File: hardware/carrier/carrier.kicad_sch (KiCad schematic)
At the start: 8 parts

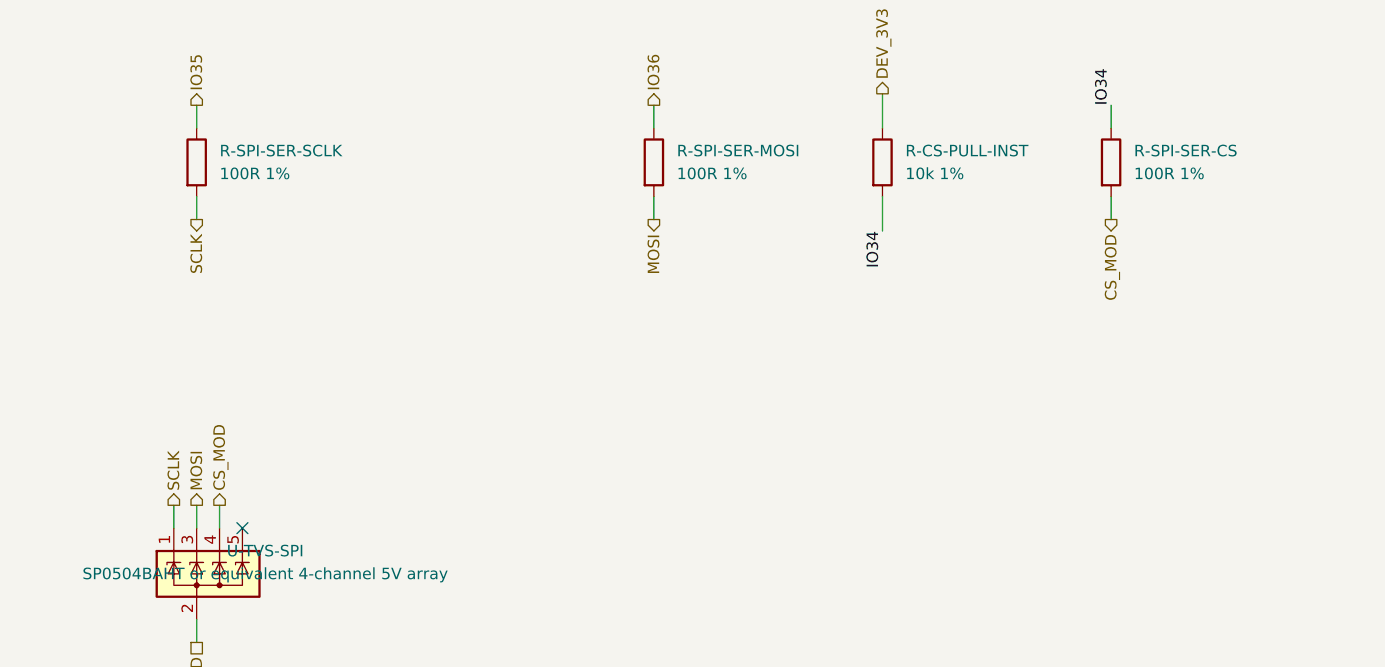
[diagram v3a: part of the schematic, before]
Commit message: WIP SPI link: U-TVS-SPI to the pad side, R-SPI-SER 82R; module receiver U-RX-MOD (74AHCT14) behind R-RX-MOD/C-RX-MOD
Co-Authored-By: Claude Opus 5.5 <noreply@anthropic.com>
Claude-Session: https://claude.ai/code/session_01LmB4muFXnoLprWX4JzuJ5A
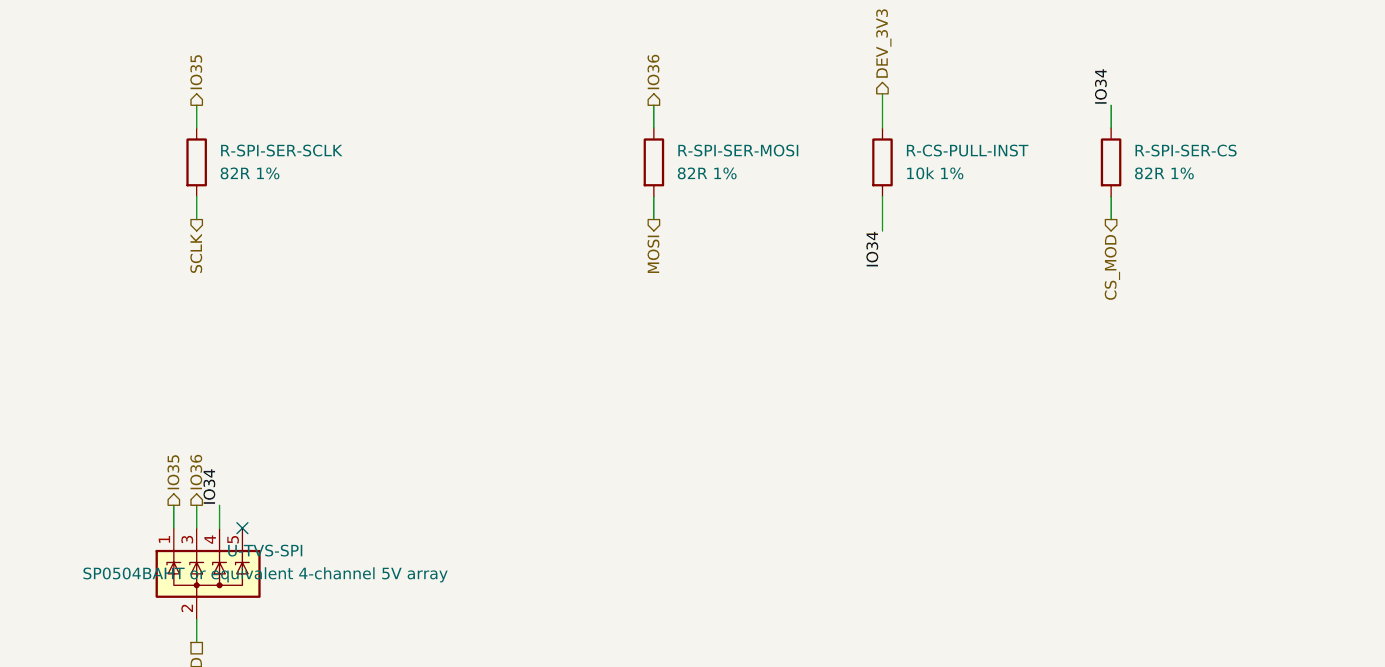
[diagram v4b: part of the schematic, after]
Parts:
- R-SPI-SER-CS, R-SPI-SER-MOSI: value 100R 1% -> 82R 1%; LCSC C17901 -> C17980; MPN 1206W4F1000T5E -> 1206W4F820JT5E
- R-SPI-SER-SCLK: value 100R 1% -> 82R 1%; LCSC C17901 -> C17980; MPN 1206W4F1000T5E -> 1206W4F820JT5E; Note At the DRIVING end, which is this board. The far end's thre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 -> At the DRIVING end, which is this board, with U-TVS-SPI on 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
- U-TVS-SPI: Note On the umbilical side of the series resistors, where the ca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 -> On the MCU side of R-SPI-SER, at the pads (owner, 2026-09-3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
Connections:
- net CS_MOD: no longer U-TVS-SPI.4 (K)
- net IO34: now also U-TVS-SPI.4 (K)
- net IO35: now also U-TVS-SPI.1 (K)
- net IO36: now also U-TVS-SPI.3 (K)
- net MOSI: no longer U-TVS-SPI.3 (K)
- net SCLK: no longer U-TVS-SPI.1 (K)
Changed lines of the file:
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@@
     (in_bom yes) (on_board yes) (dnp no)
     (property "Reference" "R-SPI-SER-SCLK" (at 43.18 232.41 0) (effects (font (size 1.27 1.27)) (justify left)))
-    (property "Value" "100R 1%" (at 43.18 234.95 0) (effects (font (size 1.27 1.27)) (justify left)))
+    (property "Value" "82R 1%" (at 43.18 234.95 0) (effects (font (size 1.27 1.27)) (justify left)))
     (property "Footprint" "Resistor_SMD:R_1206_3216Metric" (at 39.37 233.68 0) (effects (font (size 1.27 1.27)) hide))
     (property "Datasheet" "" (at 40.64 233.68 0) (effects (font (size 1.27 1.27)) hide))
@@
     (property "Pins" "1=1 2=2" (at 40.64 233.68 0) (effects (font (size 1.27 1.27)) hide))
     (property "Drawn_as" "R-SPI-SER" (at 40.64 233.68 0) (effects (font (size 1.27 1.27)) hide))
-    (property "Note" "At the DRIVING end, which is this board. The far end's threshold is the 74AHCT125's TTL V_IH, not a ratio of its rail" (at 40.64 233.68 0) (effects (font (size 1.27 1.27)) hide))
+    (property "Note" "At the DRIVING end, which is this board, with U-TVS-SPI on its pad side. The far end's receiver is the module's Schmitt stage, U-RX-MOD (74AHCT14): TTL thresholds, not a ratio of its rail" (at 40.64 233.68 0) (effects (font (size 1.27 1.27)) hide))
     (property "Manufacturer" "UNI-ROYAL" (at 40.64 233.68 0) (effects (font (size 1.27 1.27)) hide))
-    (property "MPN" "1206W4F1000T5E" (at 40.64 233.68 0) (effects (font (size 1.27 1.27)) hide))
-    (property "LCSC" "C17901" (at 40.64 233.68 0) (effects (font (size 1.27 1.27)) hide))
+    (property "MPN" "1206W4F820JT5E" (at 40.64 233.68 0) (effects (font (size 1.27 1.27)) hide))
+    (property "LCSC" "C17980" (at 40.64 233.68 0) (effects (font (size 1.27 1.27)) hide))
     (property "Assembly" "machine" (at 40.64 233.68 0) (effects (font (size 1.27 1.27)) hide))
     (pin "1")
@@
     (in_bom yes) (on_board yes) (dnp no)
     (property "Reference" "R-SPI-SER-MOSI" (at 93.98 232.41 0) (effects (font (size 1.27 1.27)) (justify left)))
-    (property "Value" "100R 1%" (at 93.98 234.95 0) (effects (font (size 1.27 1.27)) (justify left)))
+    (property "Value" "82R 1%" (at 93.98 234.95 0) (effects (font (size 1.27 1.27)) (justify left)))
     (property "Footprint" "Resistor_SMD:R_1206_3216Metric" (at 90.17 233.68 0) (effects (font (size 1.27 1.27)) hide))
     (property "Datasheet" "" (at 91.44 233.68 0) (effects (font (size 1.27 1.27)) hide))
@@
     (property "Pins" "1=1 2=2" (at 91.44 233.68 0) (effects (font (size 1.27 1.27)) hide))
     (property "Manufacturer" "UNI-ROYAL" (at 91.44 233.68 0) (effects (font (size 1.27 1.27)) hide))
-    (property "MPN" "1206W4F1000T5E" (at 91.44 233.68 0) (effects (font (size 1.27 1.27)) hide))
-    (property "LCSC" "C17901" (at 91.44 233.68 0) (effects (font (size 1.27 1.27)) hide))
+    (property "MPN" "1206W4F820JT5E" (at 91.44 233.68 0) (effects (font (size 1.27 1.27)) hide))
+    (property "LCSC" "C17980" (at 91.44 233.68 0) (effects (font (size 1.27 1.27)) hide))
     (property "Assembly" "machine" (at 91.44 233.68 0) (effects (font (size 1.27 1.27)) hide))
     (pin "1")
@@
     (in_bom yes) (on_board yes) (dnp no)
     (property "Reference" "R-SPI-SER-CS" (at 144.78 232.41 0) (effects (font (size 1.27 1.27)) (justify left)))
-    (property "Value" "100R 1%" (at 144.78 234.95 0) (effects (font (size 1.27 1.27)) (justify left)))
+    (property "Value" "82R 1%" (at 144.78 234.95 0) (effects (font (size 1.27 1.27)) (justify left)))
     (property "Footprint" "Resistor_SMD:R_1206_3216Metric" (at 140.97 233.68 0) (effects (font (size 1.27 1.27)) hide))
     (property "Datasheet" "" (at 142.24 233.68 0) (effects (font (size 1.27 1.27)) hide))
@@
     (property "Pins" "1=1 2=2" (at 142.24 233.68 0) (effects (font (size 1.27 1.27)) hide))
     (property "Manufacturer" "UNI-ROYAL" (at 142.24 233.68 0) (effects (font (size 1.27 1.27)) hide))
-    (property "MPN" "1206W4F1000T5E" (at 142.24 233.68 0) (effects (font (size 1.27 1.27)) hide))
-    (property "LCSC" "C17901" (at 142.24 233.68 0) (effects (font (size 1.27 1.27)) hide))
+    (property "MPN" "1206W4F820JT5E" (at 142.24 233.68 0) (effects (font (size 1.27 1.27)) hide))
+    (property "LCSC" "C17980" (at 142.24 233.68 0) (effects (font (size 1.27 1.27)) hide))
     (property "Assembly" "machine" (at 142.24 233.68 0) (effects (font (size 1.27 1.27)) hide))
     (pin "1")
@@
     (property "Row" "U-TVS-SPI" (at 40.64 279.4 0) (effects (font (size 1.27 1.27)) hide))
     (property "Pins" "CH1=1(K) CH2=3(K) CH3=4(K) CH4=5(K) GND=2(A)" (at 40.64 279.4 0) (effects (font (size 1.27 1.27)) hide))
-    (property "Note" "On the umbilical side of the series resistors, where the cable's energy arrives" (at 40.64 279.4 0) (effects (font (size 1.27 1.27)) hide))
+    (property "Note" "On the MCU side of R-SPI-SER, at the pads (owner, 2026-09-30): on the line side its capacitance reflected CS_MOD's returning edge back up through the far end's V_IL (cs-fall-reentry, interfaces/spi-link/sim). R-SPI-SER now stands between the cable and the clamp, and limits what a sustained fault on a conductor can push into it" (at 40.64 279.4 0) (effects (font (size 1.27 1.27)) hide))
     (property "Pins_source" "datasheets/discrete-and-power/SP0504BAHT.pdf p.1 pinout (SOT-23-5): I/O on 1, 3, 4, 5, ground on 2" (at 40.64 279.4 0) (effects (font (size 1.27 1.27)) hide))
     (property "Manufacturer" "Littelfuse" (at 40.64 279.4 0) (effects (font (size 1.27 1.27)) hide))
@@
     (property "Figure" "spi-series-r" (at 40.64 240.03 0) (effects (font (size 1.27 1.27)) hide)))
   (wire (pts (xy 38.1 274.32) (xy 38.1 271.78)) (stroke (width 0) (type default)))
-  (hierarchical_label "SCLK" (shape output) (at 38.1 271.78 90) (effects (font (size 1.27 1.27)) (justify left))
+  (hierarchical_label "IO35" (shape output) (at 38.1 271.78 90) (effects (font (size 1.27 1.27)) (justify left))
     (property "Dir" "out" (at 38.1 271.78 0) (effects (font (size 1.27 1.27)) hide))
-    (property "To" "interfaces/spi-link" (at 38.1 271.78 0) (effects (font (size 1.27 1.27)) hide))
-    (property "Figure" "spi-series-r" (at 38.1 271.78 0) (effects (font (size 1.27 1.27)) hide)))
+    (property "To" "carrier/breath-adc" (at 38.1 271.78 0) (effects (font (size 1.27 1.27)) hide)))
   (wire (pts (xy 91.44 237.49) (xy 91.44 240.03)) (stroke (width 0) (type default)))
   (hierarchical_label "MOSI" (shape output) (at 91.44 240.03 270) (effects (font (size 1.27 1.27)) (justify right))
@@
     (property "Figure" "spi-series-r" (at 91.44 240.03 0) (effects (font (size 1.27 1.27)) hide)))
   (wire (pts (xy 40.64 274.32) (xy 40.64 271.78)) (stroke (width 0) (type default)))
-  (hierarchical_label "MOSI" (shape output) (at 40.64 271.78 90) (effects (font (size 1.27 1.27)) (justify left))
+  (hierarchical_label "IO36" (shape output) (at 40.64 271.78 90) (effects (font (size 1.27 1.27)) (justify left))
     (property "Dir" "out" (at 40.64 271.78 0) (effects (font (size 1.27 1.27)) hide))
-    (property "To" "interfaces/spi-link" (at 40.64 271.78 0) (effects (font (size 1.27 1.27)) hide))
-    (property "Figure" "spi-series-r" (at 40.64 271.78 0) (effects (font (size 1.27 1.27)) hide)))
+    (property "To" "carrier/breath-adc" (at 40.64 271.78 0) (effects (font (size 1.27 1.27)) hide)))
   (wire (pts (xy 142.24 237.49) (xy 142.24 240.03)) (stroke (width 0) (type default)))
   (hierarchical_label "CS_MOD" (shape output) (at 142.24 240.03 270) (effects (font (size 1.27 1.27)) (justify right))
@@
     (property "Figure" "spi-series-r" (at 142.24 240.03 0) (effects (font (size 1.27 1.27)) hide)))
   (wire (pts (xy 43.18 274.32) (xy 43.18 271.78)) (stroke (width 0) (type default)))
-  (hierarchical_label "CS_MOD" (shape output) (at 43.18 271.78 90) (effects (font (size 1.27 1.27)) (justify left))
-    (property "Dir" "out" (at 43.18 271.78 0) (effects (font (size 1.27 1.27)) hide))
-    (property "To" "interfaces/spi-link" (at 43.18 271.78 0) (effects (font (size 1.27 1.27)) hide))
-    (property "Figure" "spi-series-r" (at 43.18 271.78 0) (effects (font (size 1.27 1.27)) hide)))
+  (label "IO34" (at 43.18 271.78 90) (fields_autoplaced) (effects (font (size 1.27 1.27)) (justify left bottom)))
   (wire (pts (xy 35.56 55.88) (xy 33.02 55.88)) (stroke (width 0) (type default)))
   (hierarchical_label "IO37" (shape input) (at 33.02 55.88 180) (effects (font (size 1.27 1.27)) (justify right))
